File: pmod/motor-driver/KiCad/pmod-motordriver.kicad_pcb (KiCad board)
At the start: 2 copper layers, 38.2 x 16.2 mm, 14 parts, among them J1 Conn_01x06_Pin, J2 Screw_Terminal_01x02, J3 Screw_Terminal_01x02, J4 Screw_Terminal_01x02, Q1 AO3401A, U1 DRV8833PWP

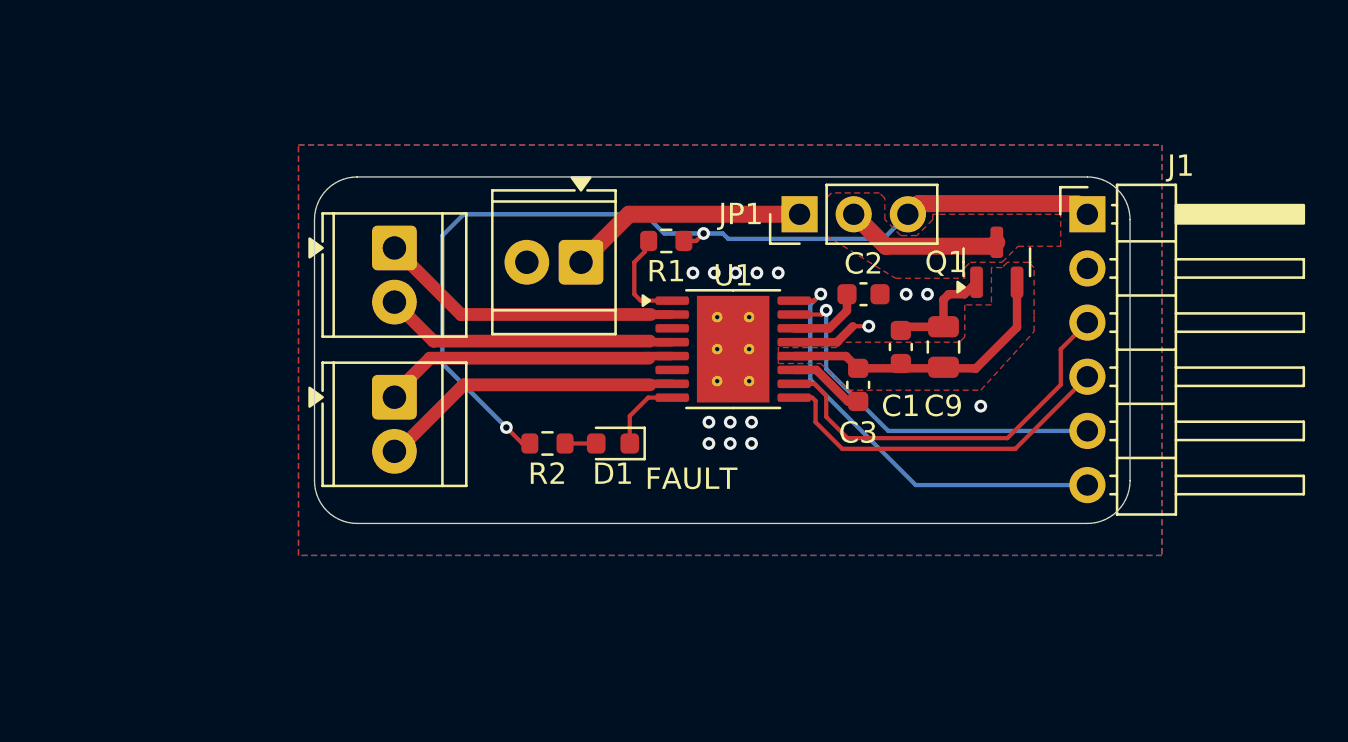
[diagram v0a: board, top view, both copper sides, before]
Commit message: update motor driver
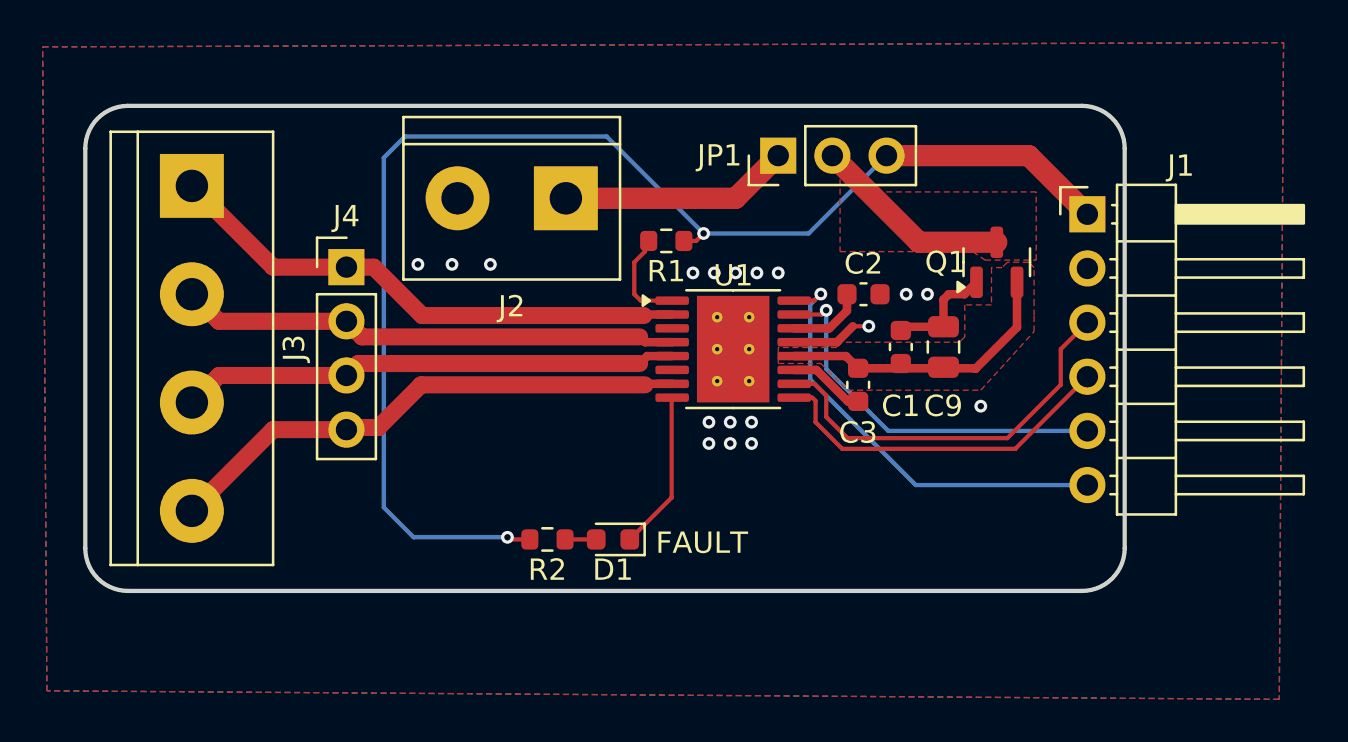
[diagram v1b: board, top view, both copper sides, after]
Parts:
- J2: footprint TerminalBlock_TE-Connectivity:TerminalBlock_TE_282834-2_1x02_P2.54mm_Horizontal -> TerminalBlock:TerminalBlock_bornier-2_P5.08mm
- J3: value Screw_Terminal_01x02 -> Screw_Terminal_01x04; footprint TerminalBlock_TE-Connectivity:TerminalBlock_TE_282834-2_1x02_P2.54mm_Horizontal -> TerminalBlock:TerminalBlock_bornier-4_P5.08mm
- J4: value Screw_Terminal_01x02 -> Conn_01x04_Pin; footprint TerminalBlock_TE-Connectivity:TerminalBlock_TE_282834-2_1x02_P2.54mm_Horizontal -> Connector_PinHeader_2.54mm:PinHeader_1x04_P2.54mm_Vertical
- moved J3 9.94 mm to (141.0, 104.9)
- moved J4 6.50 mm to (148.2, 108.7), turned to 0 degrees
- moved D1 4.50 mm to (160.8, 121.5)
- moved R2 4.50 mm to (157.7, 121.5)
- moved J2 3.08 mm to (158.5, 105.5)
- moved JP1 2.93 mm to (168.5, 103.5)
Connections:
- J3 pad 1: Net-(J3-Pin_1) -> /AOUT1
- J3 pad 2: Net-(J3-Pin_2) -> /AOUT2
- J4 pad 1: Net-(J4-Pin_1) -> /AOUT1
- J4 pad 2: Net-(J4-Pin_2) -> /AOUT2
- U1 pad 2: Net-(J3-Pin_1) -> /AOUT1
- U1 pad 4: Net-(J3-Pin_2) -> /AOUT2
- U1 pad 5: Net-(J4-Pin_1) -> /BOUT2
- U1 pad 7: Net-(J4-Pin_2) -> /BOUT1
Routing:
- net /AOUT1: track 0.00 -> 25.1 mm
- net /BOUT1: track 0.00 -> 25.0 mm
- net /AOUT2: track 0.00 -> 23.5 mm
- net /BOUT2: track 0.00 -> 23.4 mm
- net +5V: track 44.8 -> 63.7 mm
- net Net-(J3-Pin_1): track 14.3 -> 0.00 mm
- net Net-(J4-Pin_2): track 14.3 -> 0.00 mm
- net Net-(J3-Pin_2): track 14.0 -> 0.00 mm
- net Net-(J4-Pin_1): track 14.0 -> 0.00 mm
- net Net-(D1-K): track 3.63 -> 7.47 mm
- net Net-(JP1-C): track 7.41 -> 9.39 mm
- net GND: vias 15 -> 18
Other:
- board size 38.2 x 16.2 mm -> 48.8 x 22.8 mm
- board text removed: "+ MOTOR B -"
- board text removed: "- EXTERNAL +"
- board text removed: "- MOTOR A +"

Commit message: add missing silkscreen to motor driver
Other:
- board text added: "+ A - | - B +"
- board text added: "- POWER +"
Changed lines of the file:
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@@
 			(font
 				(size 1.55 1.5)
-				(thickness 0.1)
+				(thickness 0.24)
 			)
 			(justify left top mirror)
 		)
 	)
+	(gr_text "- POWER +"
+		(at 156 102.96 0)
+		(layer "B.SilkS" knockout)
+		(effects
+			(font
+				(size 1 1)
+				(thickness 0.24)
+				(bold yes)
+			)
+			(justify mirror)
+		)
+	)
+	(gr_text "+ A - | - B +"
+		(at 138 112.540001 90)
+		(layer "B.SilkS" knockout)
+		(effects
+			(font
+				(size 1 1.5)
+				(thickness 0.24)
+				(bold yes)
+			)
+			(justify mirror)
+		)
+	)
 	(gr_text "EXT POWER\nPWR SELECT\nPMOD 5V"
-		(at 172.04 108.02 90)
+		(at 171.04 106.2 90)
 		(layer "B.SilkS")
 		(effects

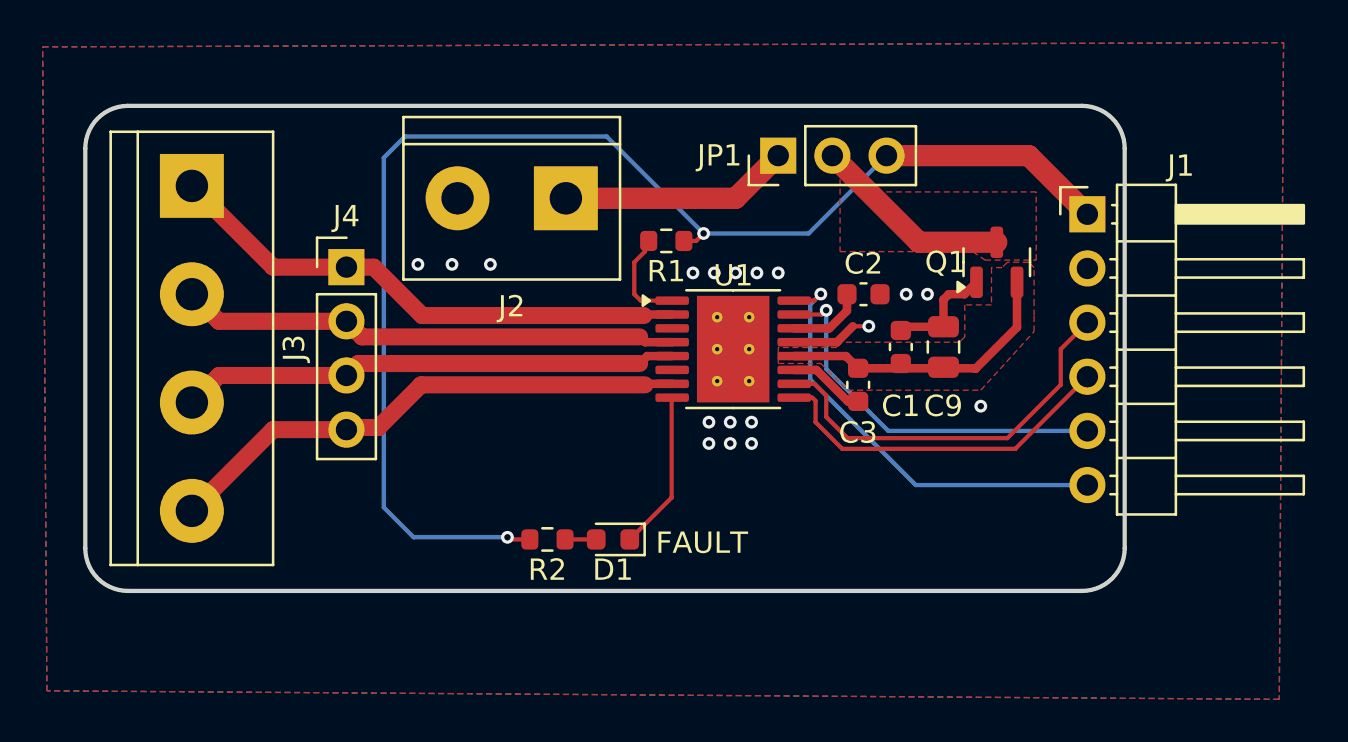
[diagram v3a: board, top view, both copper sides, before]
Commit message: polished up PCB of motor driver
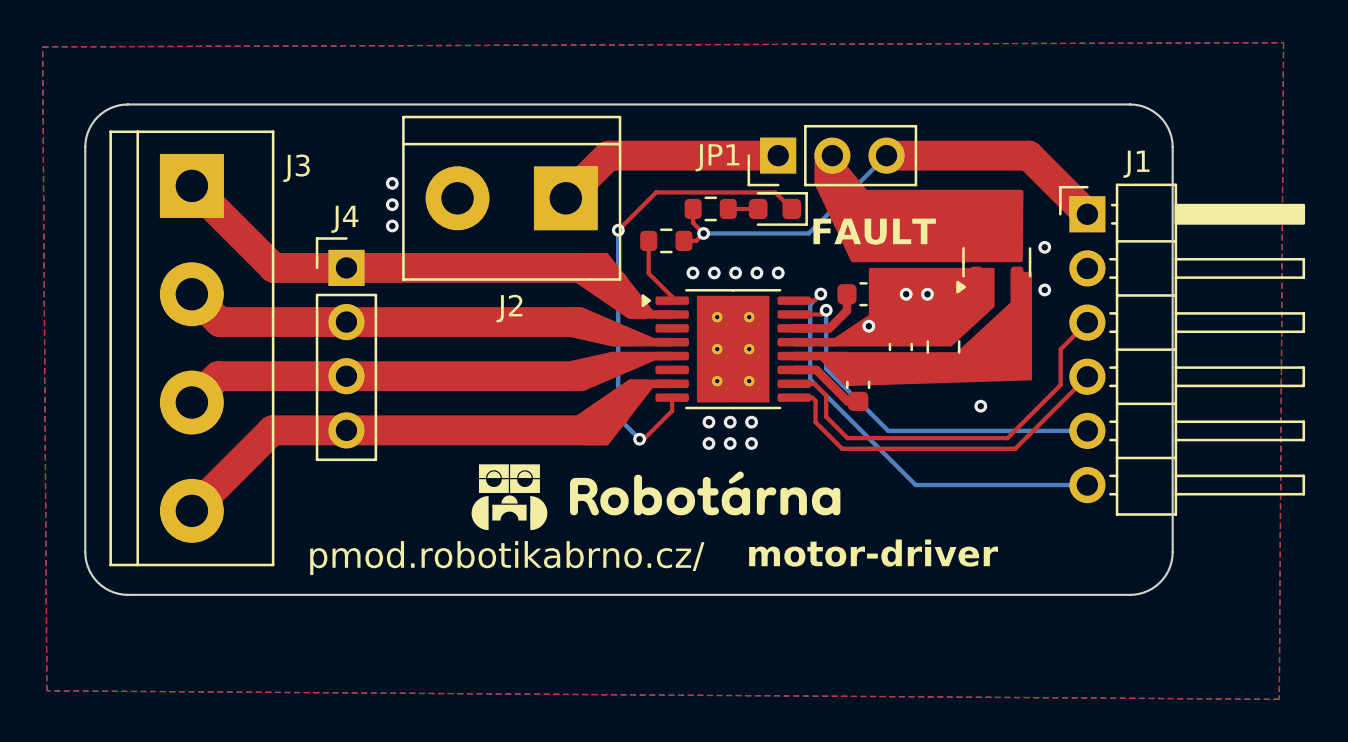
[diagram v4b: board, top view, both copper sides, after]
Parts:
- moved R2 17.3 mm to (165.3, 106.0)
- moved D1 17.3 mm to (168.3, 106.0)
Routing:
- net +5V: track 63.7 -> 23.8 mm, vias 2 -> 1
- net Net-(D1-K): track 7.47 -> 22.1 mm, vias 0 -> 2
- net Net-(JP1-C): track 9.39 -> 0.00 mm
- net /AOUT2: track 23.5 -> 21.3 mm
- net /BOUT2: track 23.4 -> 21.4 mm
- net GND: track 9.04 -> 7.23 mm, vias 18 -> 20
- net Net-(U1-~{SLEEP}): track 4.68 -> 3.26 mm
- net /AOUT1: track 25.1 -> 23.7 mm
- net /BOUT1: track 25.0 -> 23.7 mm
- removed copper zone on F.Cu, net Net-(JP1-C)
- removed copper zone on F.Cu, net VCC
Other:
- board size 48.8 x 22.8 mm -> 51 x 23 mm
- board text added: "motor-driver"
- board text added: "pmod.robotikabrno.cz/"
